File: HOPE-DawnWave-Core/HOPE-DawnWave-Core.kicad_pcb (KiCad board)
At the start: 2 copper layers, 53 parts, among them J1 USB_C_Receptacle_USB2.0_16P, J2 Screw_Terminal_01x02, SW1 RST, SW2 BOOT, U1 TLV62569DRL, U2 USBLC6-2P6, U3 ESP32-C6-WROOM-1, U4 MAX98357A, U5 BME688, X1 EYE_SPI_DISPLAY_FLIP

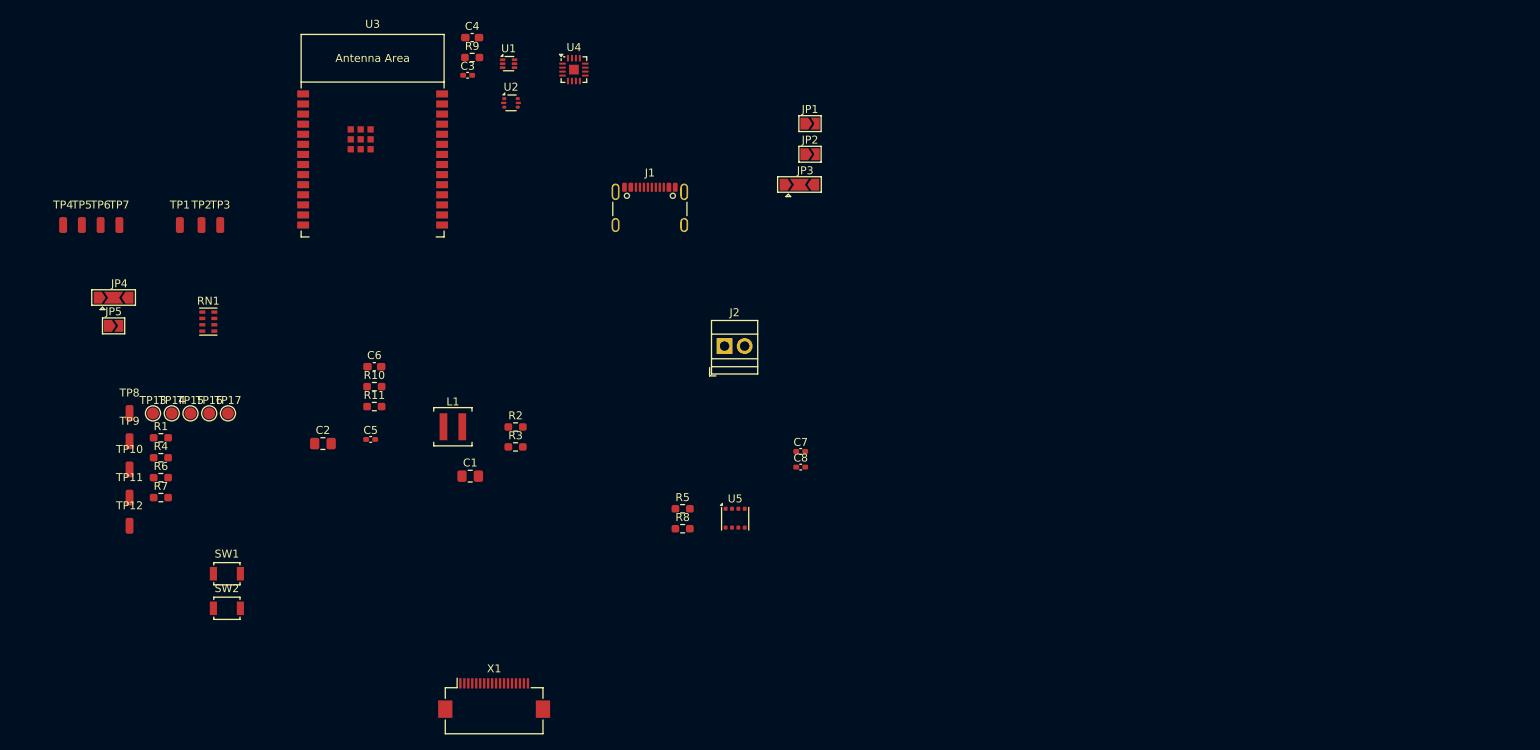
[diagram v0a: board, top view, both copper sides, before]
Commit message: positions of some components - buck converter and usb c - completed
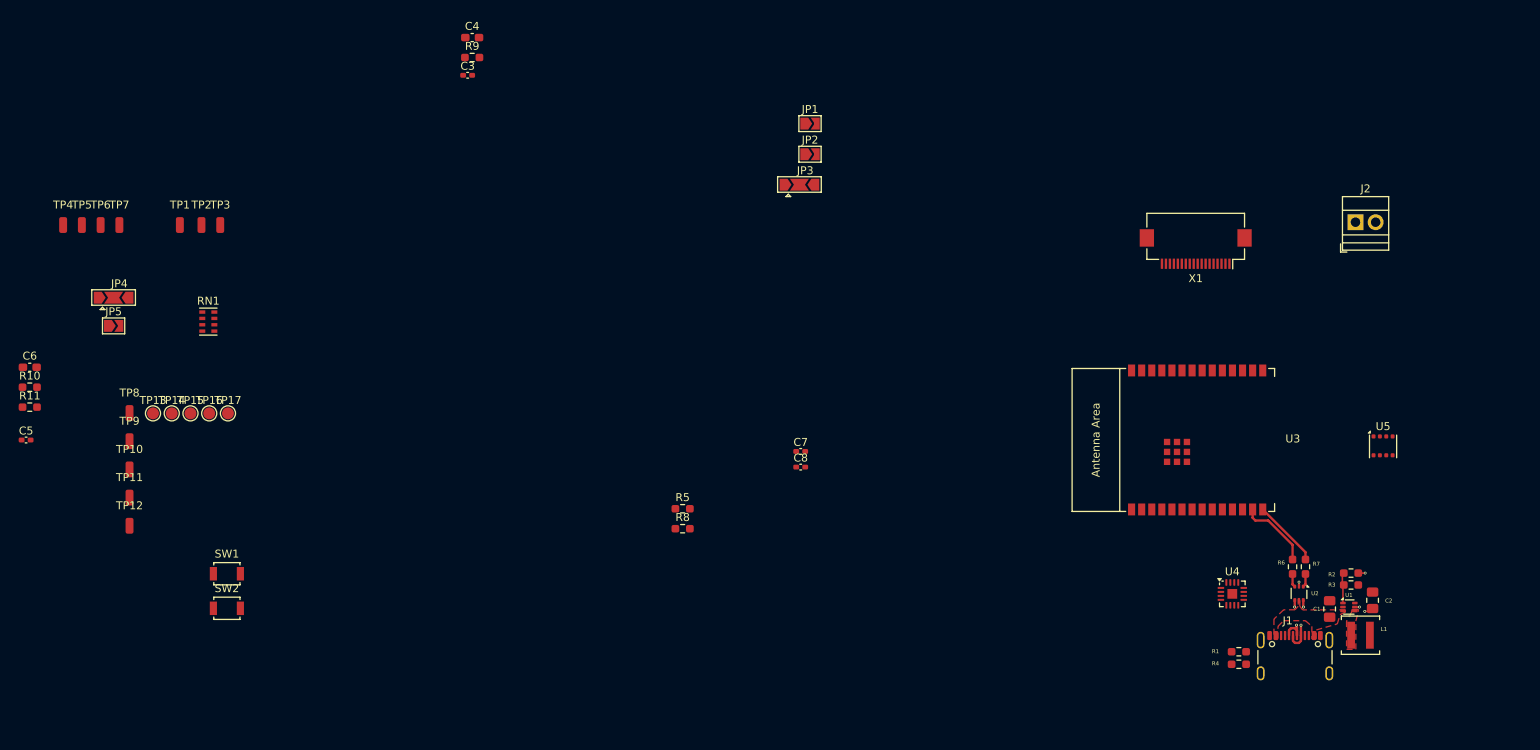
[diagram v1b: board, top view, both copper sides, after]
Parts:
- moved R7 144.4 mm to (230.6, 134.5), turned to 90 degrees
- moved R6 142.9 mm to (229.0, 134.5), turned to 90 degrees
- moved R1 138.4 mm to (222.2, 145.2), turned to 180 degrees
- moved R4 138.2 mm to (222.2, 146.7), turned to 180 degrees
- moved C2 133.6 mm to (239.1, 138.7), turned to 90 degrees
- moved U1 126.0 mm to (236.1, 139.5)
- moved L1 117.3 mm to (237.6, 143.1)
- moved U2 116.9 mm to (229.8, 137.8), turned to -90 degrees
- moved U3 109.7 mm to (217.0, 118.5), turned to 90 degrees
- moved C1 109.5 mm to (233.7, 139.8), turned to -90 degrees
- moved R2 106.8 mm to (236.4, 135.3), turned to 180 degrees
- moved R3 106.6 mm to (236.4, 136.8)
- moved U4 106.0 mm to (221.4, 137.9)
- moved X1 104.9 mm to (216.8, 94.5), turned to 180 degrees
- moved J1 98.9 mm to (229.3, 146.8)
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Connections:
- U2 pad 1: /USB_D- -> /USB_D+
- U2 pad 3: /USB_D+ -> /USB_D-
- U2 pad 4: /D+ -> /D-
- U2 pad 6: /D- -> /D+
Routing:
- net /MCU_USB_D-: track 0.00 -> 9.33 mm
- net /MCU_USB_D+: track 0.00 -> 8.53 mm
- net /D-: track 0.00 -> 4.78 mm, vias 0 -> 2
- net /D+: track 0.00 -> 4.76 mm, vias 0 -> 2
- net Net-(U1-FB): track 0.00 -> 3.82 mm
- net +3.3V: track 0.00 -> 2.01 mm, vias 0 -> 2
- net /USB_D+: track 0.00 -> 1.70 mm
- net /USB_D-: track 0.00 -> 1.70 mm
- net VBUS: track 0.00 -> 0.58 mm, vias 0 -> 1
- net GND: track 0.00 -> 0.50 mm, vias 0 -> 1
- added copper zone on F.Cu, net Net-(U1-SW)
- added copper zone on F.Cu, net VBUS

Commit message: Moved components to rough areas, not start on connecting
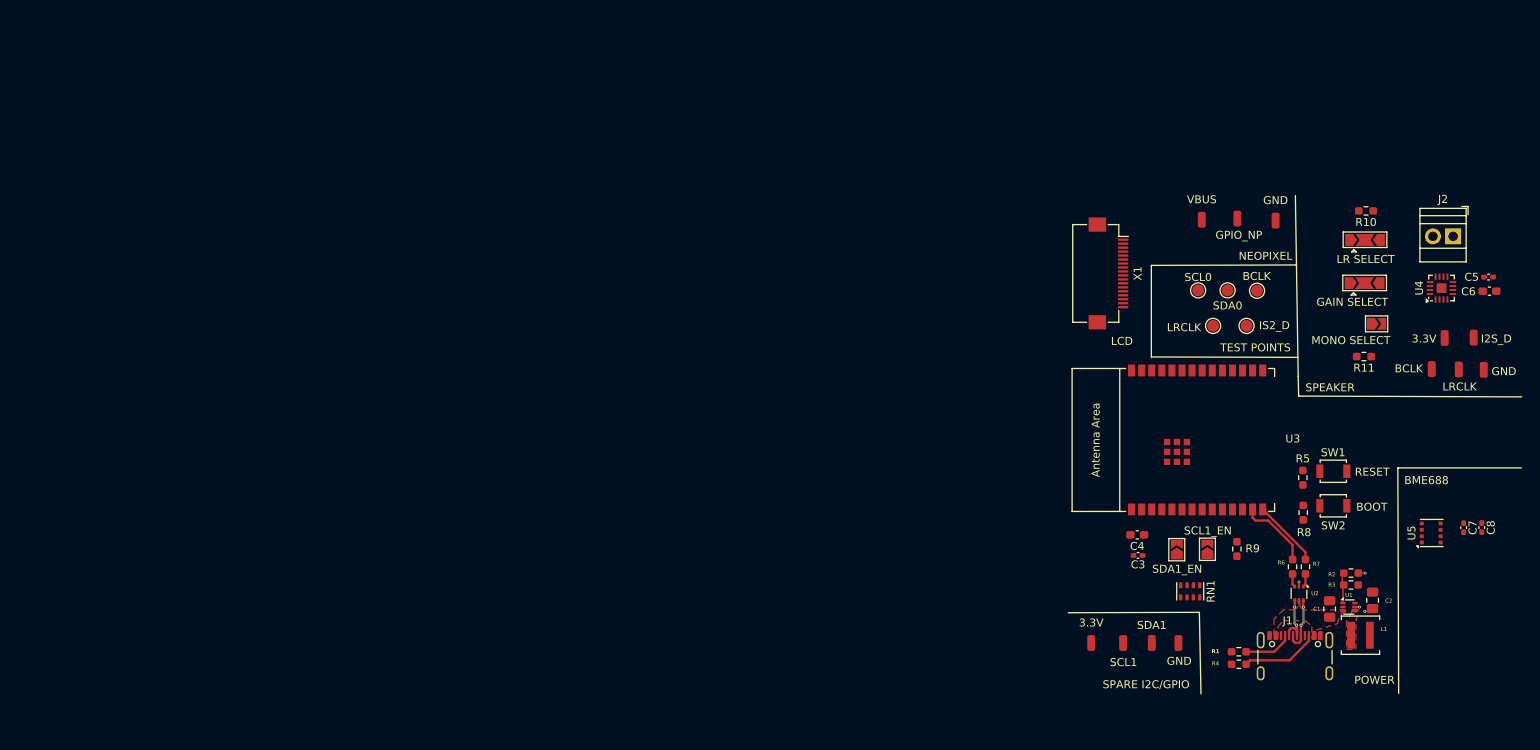
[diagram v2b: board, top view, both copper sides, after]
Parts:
- moved C5 185.3 mm to (253.7, 98.0)
- moved C6 184.0 mm to (253.8, 99.8)
- moved GND 171.7 mm to (253.1, 109.7)
- moved I2S_D 171.1 mm to (251.8, 105.6)
- moved R10 169.7 mm to (238.3, 89.7), turned to 180 degrees
- moved R11 168.1 mm to (238.0, 108.0), turned to 180 degrees
- moved LRCLK 167.6 mm to (249.9, 109.6)
- moved BCLK 164.1 mm to (246.5, 109.6)
- moved JP5 159.0 mm to (239.6, 103.9)
- moved JP4 157.5 mm to (238.1, 98.8)
- moved 3.3V 154.8 mm to (248.2, 105.7)
- moved GND 147.7 mm to (226.9, 90.9)
- moved SDA1 144.6 mm to (211.3, 144.1)
- moved SCL1 143.5 mm to (207.7, 144.1)
- moved GPIO_NP 143.1 mm to (222.0, 90.6)
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- renumbered TP3 to 3.3V, TP2 to 3.3V, TP8 to BCLK, TP15 to BCLK, TP12 to GND, TP10 to GND, TP11 to GND, TP6 to GPIO_NP, TP7 to I2S_D, TP17 to IS2_D, TP9 to LRCLK, TP16 to LRCLK, TP13 to SCL0, TP4 to SCL1, JP1 to SCL1_EN, TP14 to SDA0, TP5 to SDA1, JP2 to SDA1_EN, TP1 to VBUS
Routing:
- net Net-(J1-CC2): track 0.00 -> 9.80 mm
- net Net-(J1-CC1): track 0.00 -> 6.15 mm
- net /D+: track 4.76 -> 7.16 mm
- net /D-: track 4.78 -> 7.16 mm
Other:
- board text added: "BME688"
- board text added: "BOOT"
- board text added: "GAIN SELECT"
- board text added: "LCD"
- board text added: "LR SELECT"
- board text added: "MONO SELECT"
- board text added: "NEOPIXEL"
- board text added: "POWER"
- board text added: "RESET"
- board text added: "SPARE I2C/GPIO"
- board text added: "SPEAKER"
- board text added: "TEST POINTS"

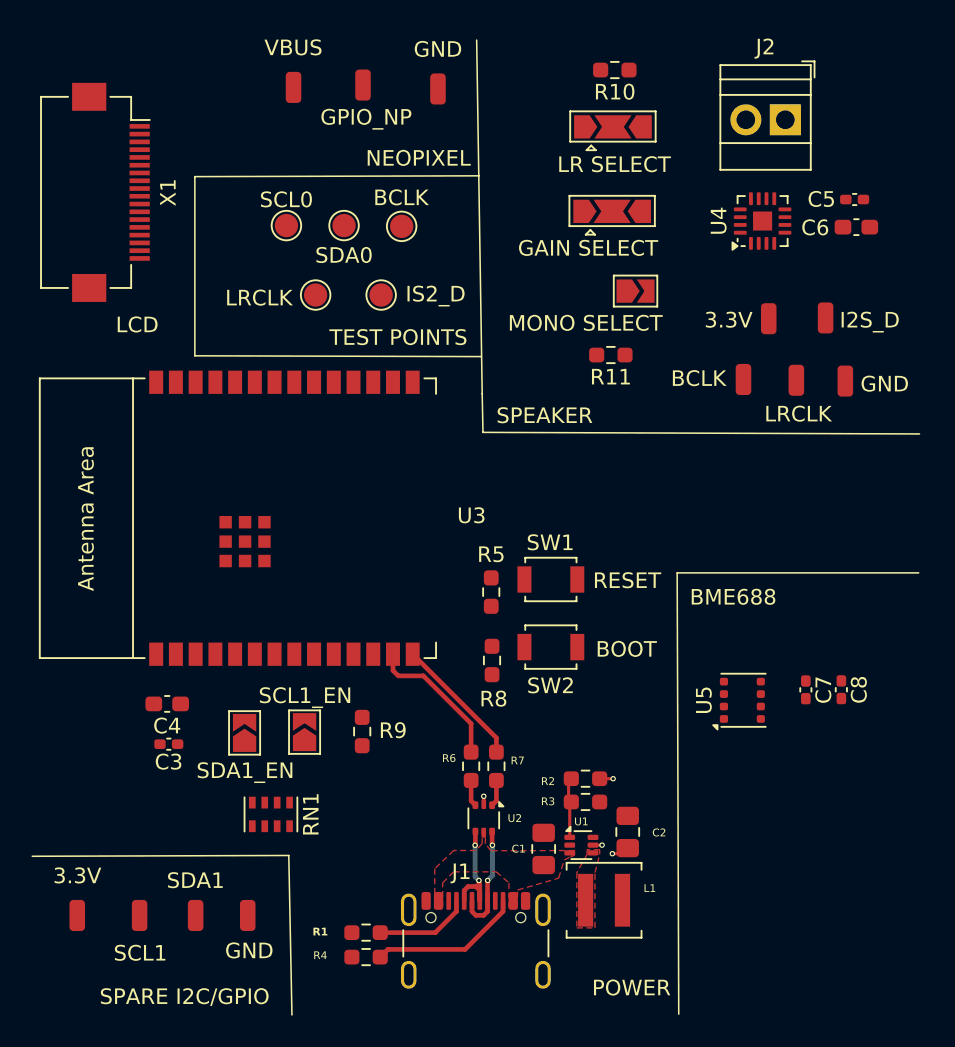
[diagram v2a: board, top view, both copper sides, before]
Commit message: flipped esp32 to keep 3.3v on right and 5v on left
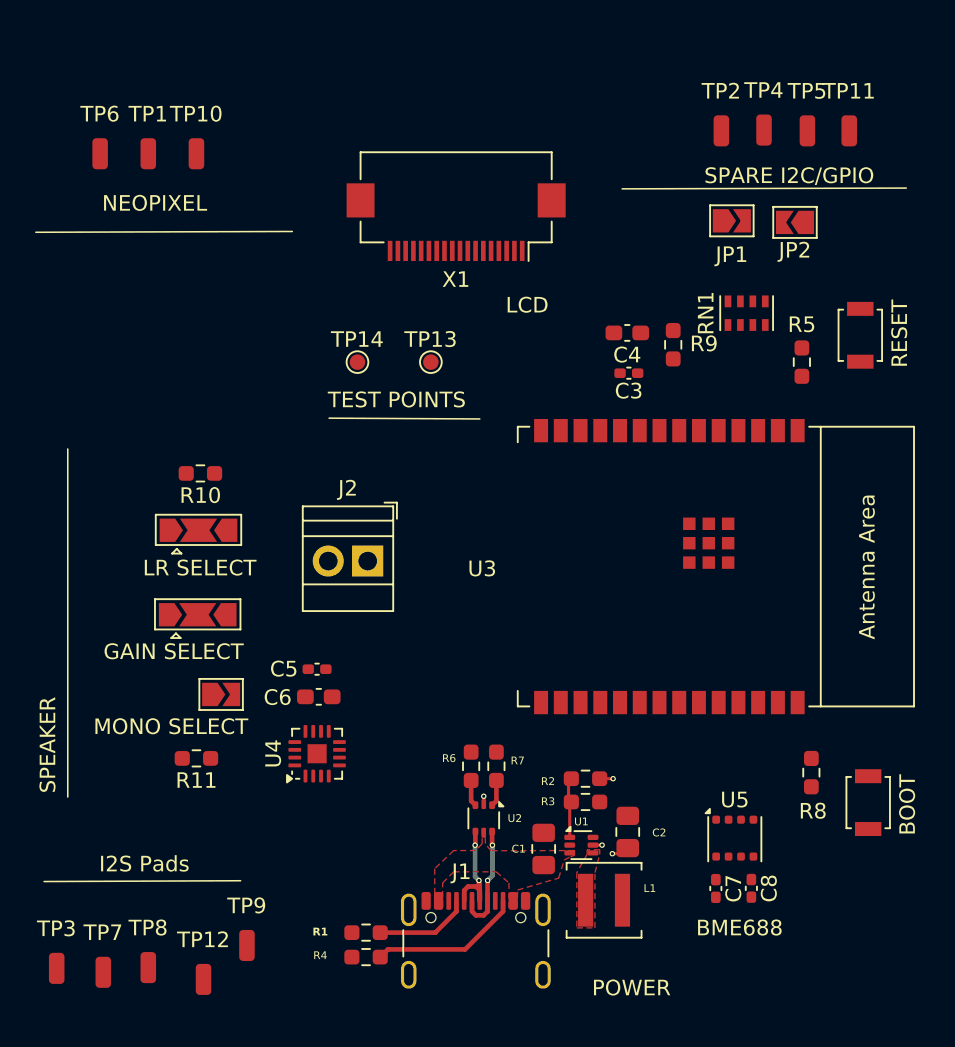
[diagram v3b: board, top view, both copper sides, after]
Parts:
- removed 3.3V (x2): +3.3V, Connector_Wire:SolderWirePad_1x01_SMD_1x2mm
- removed BCLK: BCLK, Connector_Wire:SolderWirePad_1x01_SMD_1x2mm
- removed BCLK: BCLK, TestPoint:TestPoint_Pad_D1.5mm
- removed GND (x3): GND, Connector_Wire:SolderWirePad_1x01_SMD_1x2mm
- removed GPIO_NP: NP, Connector_Wire:SolderWirePad_1x01_SMD_1x2mm
- removed I2S_D: I2S_D, Connector_Wire:SolderWirePad_1x01_SMD_1x2mm
- removed IS2_D: I2S_D, TestPoint:TestPoint_Pad_D1.5mm
- removed LRCLK: LRCLK, Connector_Wire:SolderWirePad_1x01_SMD_1x2mm
- removed LRCLK: LRCLK, TestPoint:TestPoint_Pad_D1.5mm
- removed SCL0: SCL0, TestPoint:TestPoint_Pad_D1.5mm
- removed SCL1: SCL1, Connector_Wire:SolderWirePad_1x01_SMD_1x2mm
- removed SCL1_EN, SDA1_EN: PU, Jumper:SolderJumper-2_P1.3mm_Open_TrianglePad1.0x1.5mm
- removed SDA0: SDA0, TestPoint:TestPoint_Pad_D1.5mm
- removed SDA1: SDA1, Connector_Wire:SolderWirePad_1x01_SMD_1x2mm
- removed VBUS: +5V, Connector_Wire:SolderWirePad_1x01_SMD_1x2mm
- added JP1: PU, Jumper:SolderJumper-2_P1.3mm_Open_TrianglePad1.0x1.5mm, F.Cu at (245.8, 99.4)
- added JP2: PU, Jumper:SolderJumper-2_P1.3mm_Open_TrianglePad1.0x1.5mm, F.Cu at (249.8, 99.5)
- added TP1: +5V, Connector_Wire:SolderWirePad_1x01_SMD_1x2mm, F.Cu at (208.2, 95.0)
- added TP10: GND, Connector_Wire:SolderWirePad_1x01_SMD_1x2mm, F.Cu at (211.3, 95.0)
- added TP11: GND, Connector_Wire:SolderWirePad_1x01_SMD_1x2mm, F.Cu at (253.3, 93.6)
- added TP12: GND, Connector_Wire:SolderWirePad_1x01_SMD_1x2mm, F.Cu at (211.8, 148.2)
- added TP13: SCL0, TestPoint:TestPoint_Pad_D1.0mm, F.Cu at (226.4, 108.5)
- added TP14: SDA0, TestPoint:TestPoint_Pad_D1.0mm, F.Cu at (221.7, 108.5)
- added TP2: +3.3V, Connector_Wire:SolderWirePad_1x01_SMD_1x2mm, F.Cu at (245.1, 93.6)
- added TP3: +3.3V, Connector_Wire:SolderWirePad_1x01_SMD_1x2mm, F.Cu at (202.3, 147.5)
- added TP4: SCL1, Connector_Wire:SolderWirePad_1x01_SMD_1x2mm, F.Cu at (247.9, 93.5)
- added TP5: SDA1, Connector_Wire:SolderWirePad_1x01_SMD_1x2mm, F.Cu at (250.6, 93.6)
- added TP6: NP, Connector_Wire:SolderWirePad_1x01_SMD_1x2mm, F.Cu at (205.1, 95.0)
- added TP7: I2S_D, Connector_Wire:SolderWirePad_1x01_SMD_1x2mm, F.Cu at (205.3, 147.7)
- added TP8: BCLK, Connector_Wire:SolderWirePad_1x01_SMD_1x2mm, F.Cu at (208.2, 147.4)
- added TP9: LRCLK, Connector_Wire:SolderWirePad_1x01_SMD_1x2mm, F.Cu at (214.6, 146.0)
- moved C5 45.9 mm to (219.1, 128.2)
- moved C6 45.9 mm to (219.2, 130.0)
- moved U4 44.7 mm to (219.1, 133.7)
- moved RN1 44.5 mm to (246.7, 105.3), turned to 90 degrees
- moved J2 39.1 mm to (222.4, 121.3)
- moved C3 38.0 mm to (239.2, 109.2)
- moved C4 38.0 mm to (239.1, 106.6)
- moved JP4 37.2 mm to (211.4, 124.7)
- moved JP5 37.2 mm to (212.9, 129.8)
- moved JP3 37.2 mm to (211.5, 119.3)
- moved R10 37.2 mm to (211.6, 115.6)
- moved R11 37.2 mm to (211.3, 134.0)
- moved R9 31.9 mm to (242.0, 107.3)
- moved SW1 25.4 mm to (254.1, 106.7), turned to -90 degrees
- moved U3 25.0 mm to (241.8, 121.6), turned to -90 degrees
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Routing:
- net /MCU_USB_D-: track 9.33 -> 0.00 mm
- net /MCU_USB_D+: track 8.53 -> 0.00 mm
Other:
- board text added: "I2S Pads"
